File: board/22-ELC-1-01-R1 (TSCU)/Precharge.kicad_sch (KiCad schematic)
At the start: 5 parts, among them J8 Conn_01x01, Q9 Q_NMOS_DGS

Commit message: Ready for review
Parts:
- renumbered D7 to D11, J8 to J10, Q9 to Q8, R42 to R33
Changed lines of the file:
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@@
   (symbol (lib_id "Device:Q_NMOS_GSD") (at 149.86 134.62 0) (unit 1)
     (in_bom yes) (on_board yes)
-    (property "Reference" "Q9" (id 0) (at 139.7 140.97 0)
+    (property "Reference" "Q8" (id 0) (at 139.7 140.97 0)
       (effects (font (size 1.27 1.27)) (justify left))
     )
@@
   (symbol (lib_id "Connector_Generic:Conn_01x02") (at 143.51 120.65 0) (mirror y) (unit 1)
     (in_bom yes) (on_board yes)
-    (property "Reference" "J8" (id 0) (at 141.478 119.5832 0)
+    (property "Reference" "J10" (id 0) (at 141.478 119.5832 0)
       (effects (font (size 1.27 1.27)) (justify left))
     )
@@
   (symbol (lib_id "Device:D_TVS") (at 158.75 121.92 270) (unit 1)
     (in_bom yes) (on_board yes)
-    (property "Reference" "D7" (id 0) (at 160.782 120.7516 90)
+    (property "Reference" "D11" (id 0) (at 160.782 120.7516 90)
       (effects (font (size 1.27 1.27)) (justify left))
     )
@@
   (symbol (lib_id "Device:R") (at 132.08 134.62 270) (unit 1)
     (in_bom yes) (on_board yes)
-    (property "Reference" "R42" (id 0) (at 132.08 132.08 90))
+    (property "Reference" "R33" (id 0) (at 132.08 132.08 90))
     (property "Value" "10k" (id 1) (at 132.08 134.62 90))
     (property "Footprint" "Resistor_SMD:R_0603_1608Metric_Pad0.98x0.95mm_HandSolder" (id 2) (at 132.08 132.842 90)

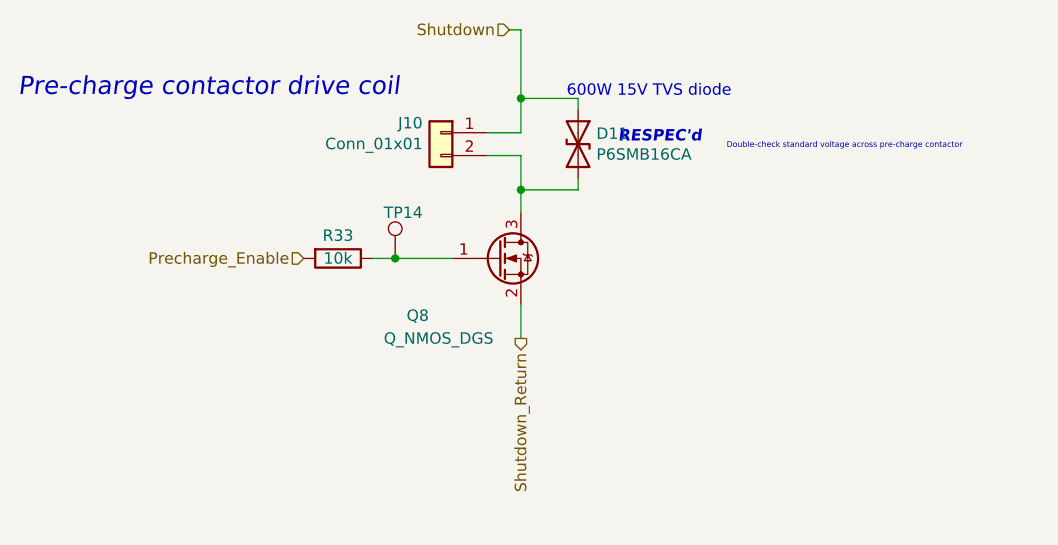
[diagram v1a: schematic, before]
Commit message: All good except need to switch everything to accepting 24v power
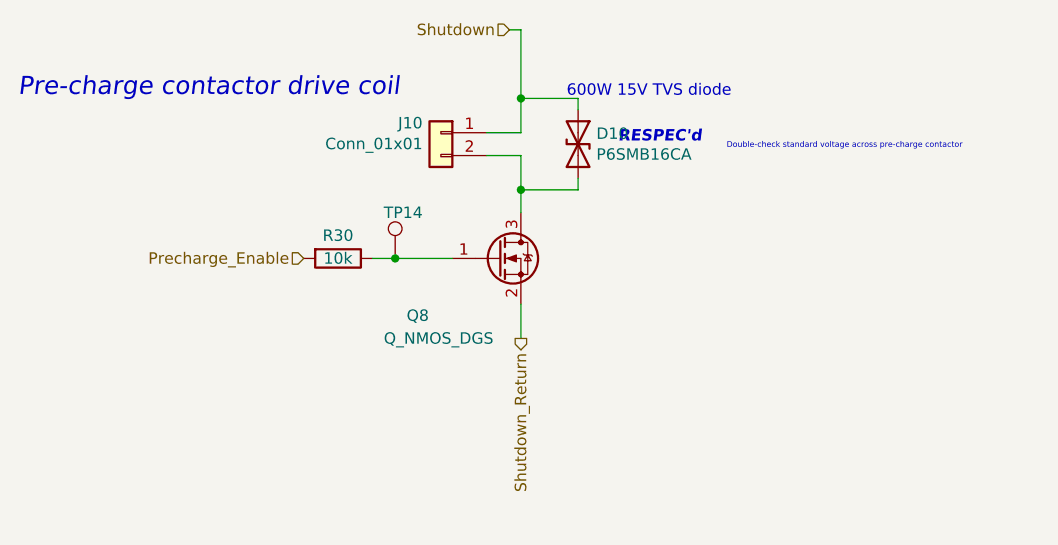
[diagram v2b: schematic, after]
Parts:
- renumbered D11 to D10, R33 to R30
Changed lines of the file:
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@@
   (symbol (lib_id "Device:D_TVS") (at 158.75 121.92 270) (unit 1)
     (in_bom yes) (on_board yes)
-    (property "Reference" "D11" (id 0) (at 160.782 120.7516 90)
+    (property "Reference" "D10" (id 0) (at 160.782 120.7516 90)
       (effects (font (size 1.27 1.27)) (justify left))
     )
@@
   (symbol (lib_id "Device:R") (at 132.08 134.62 270) (unit 1)
     (in_bom yes) (on_board yes)
-    (property "Reference" "R33" (id 0) (at 132.08 132.08 90))
+    (property "Reference" "R30" (id 0) (at 132.08 132.08 90))
     (property "Value" "10k" (id 1) (at 132.08 134.62 90))
     (property "Footprint" "Resistor_SMD:R_0603_1608Metric_Pad0.98x0.95mm_HandSolder" (id 2) (at 132.08 132.842 90)

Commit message: Finalized schematic, started board layout
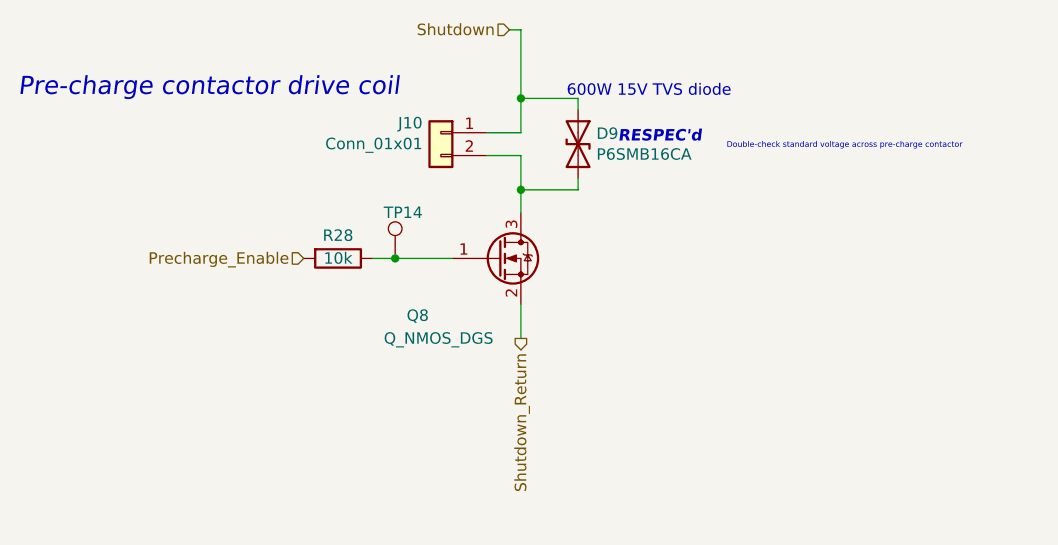
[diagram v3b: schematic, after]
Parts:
- R28: renamed from R30; footprint Resistor_SMD:R_0603_1608Metric_Pad0.98x0.95mm_HandSolder -> FixedTextSizes:R_0402_1005Metric
- renumbered D10 to D9
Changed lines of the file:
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@@
   (symbol (lib_id "Device:D_TVS") (at 158.75 121.92 270) (unit 1)
     (in_bom yes) (on_board yes)
-    (property "Reference" "D10" (id 0) (at 160.782 120.7516 90)
+    (property "Reference" "D9" (id 0) (at 160.782 120.7516 90)
       (effects (font (size 1.27 1.27)) (justify left))
     )
@@
   (symbol (lib_id "Device:R") (at 132.08 134.62 270) (unit 1)
     (in_bom yes) (on_board yes)
-    (property "Reference" "R30" (id 0) (at 132.08 132.08 90))
+    (property "Reference" "R28" (id 0) (at 132.08 132.08 90))
     (property "Value" "10k" (id 1) (at 132.08 134.62 90))
-    (property "Footprint" "Resistor_SMD:R_0603_1608Metric_Pad0.98x0.95mm_HandSolder" (id 2) (at 132.08 132.842 90)
+    (property "Footprint" "FixedTextSizes:R_0402_1005Metric" (id 2) (at 132.08 132.842 90)
       (effects (font (size 1.27 1.27)) hide)
     )

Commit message: More progress
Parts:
- renumbered J10 to J11
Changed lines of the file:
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@@
   (symbol (lib_id "Connector_Generic:Conn_01x02") (at 143.51 120.65 0) (mirror y) (unit 1)
     (in_bom yes) (on_board yes)
-    (property "Reference" "J10" (id 0) (at 141.478 119.5832 0)
+    (property "Reference" "J11" (id 0) (at 141.478 119.5832 0)
       (effects (font (size 1.27 1.27)) (justify left))
     )
